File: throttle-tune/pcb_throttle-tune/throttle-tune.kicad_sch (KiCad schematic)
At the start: 48 parts, among them IC1 ATMEGA8A-P, J1 Screw_Terminal_01x03, J10 9V supply / small battery, J2 Screw_Terminal_01x03, J3 Screw_Terminal_01x03, J4 Screw_Terminal_01x03, J5 Conn_01x03_Pin, J6 UART, J7 gpio-reserve, J8 gpio-reserve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

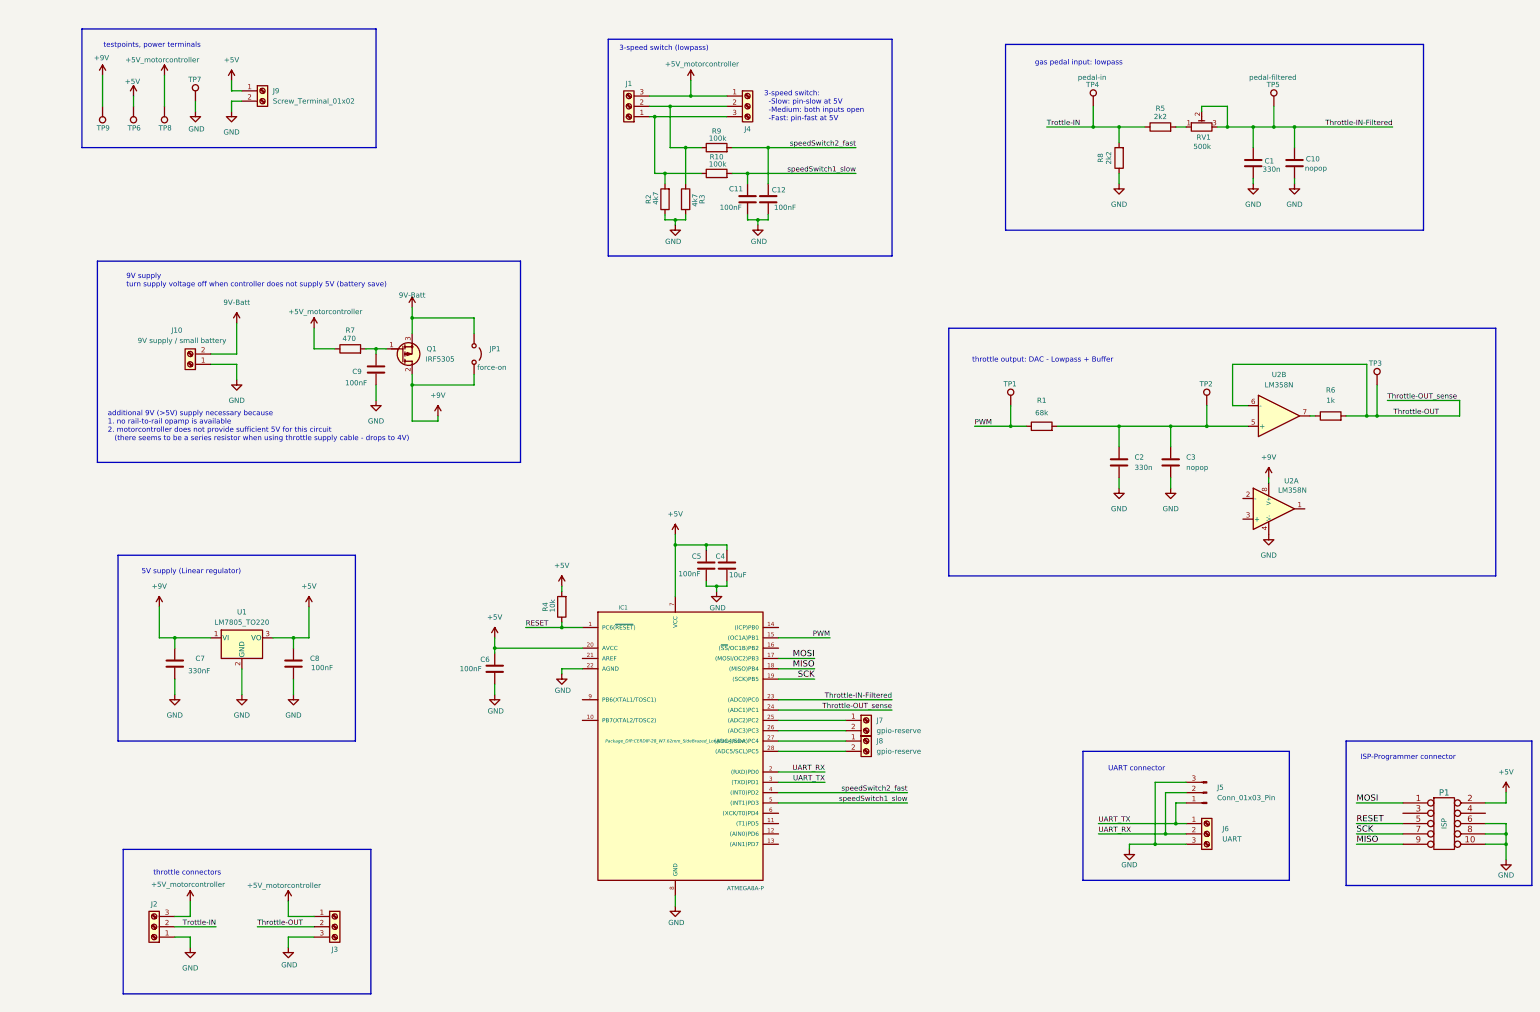
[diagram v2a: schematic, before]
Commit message: pcb: arrange components
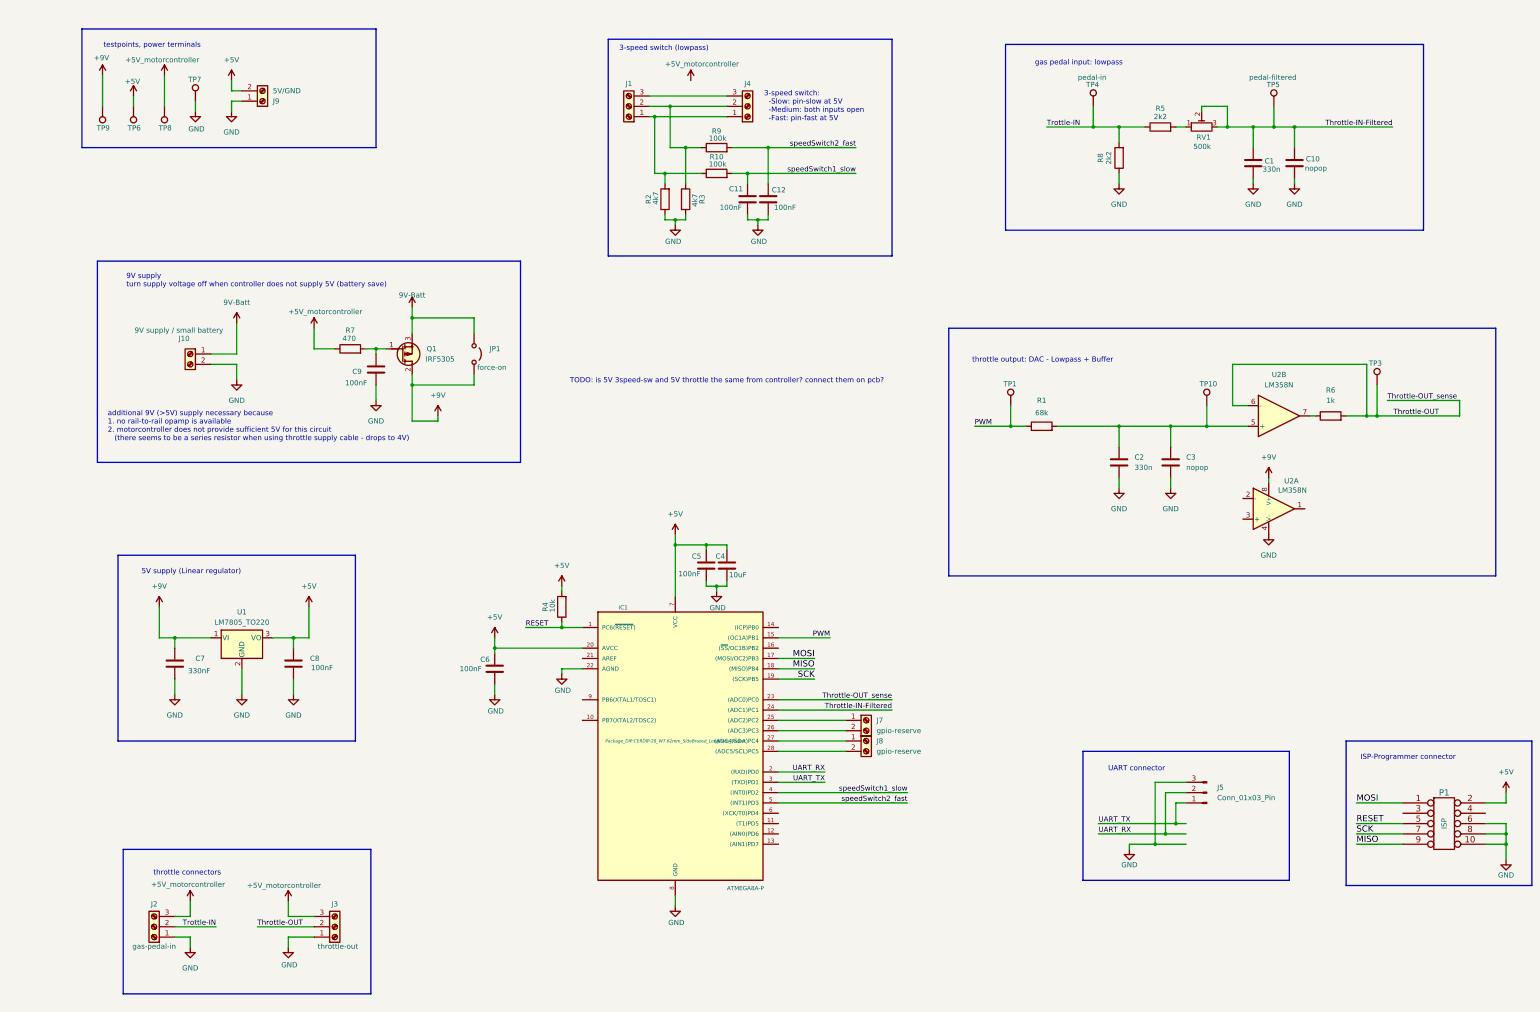
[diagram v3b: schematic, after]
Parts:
- removed J6: UART, TerminalBlock:TerminalBlock_bornier-2_P5.08mm, symbol Connector:Screw_Terminal_01x03
- J1: value Screw_Terminal_01x03 -> 3speedSw-in
- J2: value Screw_Terminal_01x03 -> gas-pedal-in
- J3: value Screw_Terminal_01x03 -> throttle-out
- J4: value Screw_Terminal_01x03 -> 3speedSw-out
- J5: footprint Connector_PinHeader_1.00mm:PinHeader_1x03_P1.00mm_Vertical -> Connector_PinHeader_2.54mm:PinHeader_1x03_P2.54mm_Vertical
- J9: value Screw_Terminal_01x02 -> 5V/GND
- JP1: footprint Connector_PinHeader_1.00mm:PinHeader_1x02_P1.00mm_Vertical -> Jumper_AKL:Jumper_P2.54mm_D0.7mm
- Q1: footprint Package_TO_SOT_THT:TO-220F-3_Vertical -> Package_TO_SOT_THT:TO-220-3_Vertical
- RV1: footprint Resistor_THT:R_Axial_DIN0207_L6.3mm_D2.5mm_P10.16mm_Horizontal -> Potentiometer_THT:Potentiometer_Piher_PT-10-V10_Vertical
- TP1: value TestPoint -> PWM
- TP10: renamed from TP2; value TestPoint -> DAC
- TP3: value TestPoint -> Throttle-Out
- TP7: value TestPoint -> GND
- TP8: value TestPoint -> 5V controller
- TP9: value TestPoint -> 9V
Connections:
- net +5V: now also J9.2 (Pin_2); no longer J9.1 (Pin_1)
- net +5V_motorcontroller: now also J3.3 (Pin_3); no longer J1.3 (Pin_3), J3.1 (Pin_1), J4.1 (Pin_1)
- net 9V-Batt: now also J10.1 (Pin_1); no longer J10.2 (Pin_2)
- net GND: now also J10.2 (Pin_2), J3.1 (Pin_1), J9.1 (Pin_1); no longer J10.1 (Pin_1), J3.3 (Pin_3), J9.2 (Pin_2)
- net Throttle-IN-Filtered: now also IC1.24 ((ADC1)PC1); no longer IC1.23 ((ADC0)PC0)
- net Throttle-OUT: now also IC1.23 ((ADC0)PC0); no longer IC1.24 ((ADC1)PC1)
- net speedSwitch1_slow: now also IC1.4 ((INT0)PD2); no longer IC1.5 ((INT1)PD3)
- net speedSwitch2_fast: now also IC1.5 ((INT1)PD3); no longer IC1.4 ((INT0)PD2)
- net at J1.1 (Pin_1), R10.1, R2.2: now also J4.1 (Pin_1); no longer J4.3 (Pin_3)
- new net: J1.3 (Pin_3), J4.3 (Pin_3)
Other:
- note added: "TODO: is 5V 3speed-sw and 5V throttle the same from controller? connect them on pcb?"
- moved on the sheet: J10
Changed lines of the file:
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@@
 	)
 	(junction
-		(at 172.72 38.1)
-		(diameter 0)
-		(color 0 0 0 0)
-	)
-	(junction
 		(at 104.14 109.22)
 		(diameter 0)
@@
 	(wire
 		(pts
-			(xy 172.72 34.29) (xy 172.72 38.1)
-		)
-		(stroke
-			(width 0)
-			(type default)
-		)
-	)
-	(wire
-		(pts
 			(xy 278.13 45.72) (xy 278.13 49.53)
 		)
@@
 	(wire
 		(pts
-			(xy 162.56 38.1) (xy 172.72 38.1)
+			(xy 162.56 38.1) (xy 181.61 38.1)
 		)
 		(stroke
@@
 	(wire
 		(pts
-			(xy 172.72 38.1) (xy 181.61 38.1)
-		)
-		(stroke
-			(width 0)
-			(type default)
-		)
-	)
-	(wire
-		(pts
 			(xy 186.69 68.58) (xy 189.23 68.58)
 		)
@@
 		)
 	)
+	(text "TODO: is 5V 3speed-sw and 5V throttle the same from controller? connect them on pcb?"
+		(exclude_from_sim no)
+		(at 181.61 108.204 0)
+		(effects
+			(font
+				(size 1.27 1.27)
+			)
+		)
+	)
 	(text "throttle connectors\n"
 		(exclude_from_sim no)
@@
 	)
 	(label "speedSwitch1_slow"
-		(at 226.06 212.09 180)
+		(at 226.06 209.55 180)
 		(fields_autoplaced yes)
 		(effects
@@
 	)
 	(label "speedSwitch2_fast"
-		(at 226.06 209.55 180)
+		(at 226.06 212.09 180)
 		(fields_autoplaced yes)
 		(effects
@@
 	)
 	(label "Throttle-IN-Filtered"
-		(at 222.25 186.69 180)
+		(at 222.25 189.23 180)
 		(fields_autoplaced yes)
 		(effects
@@
 	)
 	(label "Throttle-OUT_sense"
-		(at 222.25 189.23 180)
+		(at 222.25 186.69 180)
 		(fields_autoplaced yes)
 		(effects
@@
 			)
 		)
-		(property "Value" "TestPoint"
+		(property "Value" "5V controller"
 			(at 46.99 47.244 0)
 			(effects
@@
 		(on_board yes)
 		(dnp no)
-		(property "Reference" "TP2"
+		(property "Reference" "TP10"
 			(at 297.942 108.966 0)
 			(effects
@@
 			)
 		)
-		(property "Value" "TestPoint"
+		(property "Value" "DAC"
 			(at 302.26 112.2679 0)
 			(effects
@@
 			(project "throttle-tune"
 				(path "/54596f3c-134d-419d-8b8d-e3d4fb1ac7e3"
-					(reference "TP2")
+					(reference "TP10")
 					(unit 1)
 				)
@@
 	(symbol
 		(lib_id "Connector:Screw_Terminal_01x02")
-		(at 67.31 36.83 0)
+		(at 67.31 39.37 0)
+		(mirror x)
 		(unit 1)
 		(exclude_from_sim no)
@@
 		(on_board yes)
 		(dnp no)
-		(fields_autoplaced yes)
 		(property "Reference" "J9"
-			(at 69.85 36.8299 0)
+			(at 69.85 39.3701 0)
 			(effects
 				(font
@@
 			)
 		)
-		(property "Value" "Screw_Terminal_01x02"
-			(at 69.85 39.3699 0)
+		(property "Value" "5V/GND"
+			(at 69.85 36.8301 0)
 			(effects
 				(font
@@
 		)
 		(property "Footprint" "TerminalBlock:TerminalBlock_bornier-2_P5.08mm"
-			(at 67.31 36.83 0)
+			(at 67.31 39.37 0)
 			(effects
 				(font
@@
 		)
 		(property "Datasheet" "~"
-			(at 67.31 36.83 0)
+			(at 67.31 39.37 0)
 			(effects
 				(font
@@
 		)
 		(property "Description" "Generic screw terminal, single row, 01x02, script generated (kicad-library-utils/schlib/autogen/connector/)"
-			(at 67.31 36.83 0)
+			(at 67.31 39.37 0)
 			(effects
 				(font
@@
 			)
 		)
-		(property "Footprint" "Package_TO_SOT_THT:TO-220F-3_Vertical"
+		(property "Footprint" "Package_TO_SOT_THT:TO-220-3_Vertical"
 			(at 106.68 104.14 0)
 			(effects
@@
 	)
 	(symbol
-		(lib_id "Connector:Screw_Terminal_01x03")
-		(at 299.72 219.71 0)
-		(unit 1)
-		(exclude_from_sim no)
-		(in_bom yes)
-		(on_board yes)
-		(dnp no)
-		(fields_autoplaced yes)
-		(property "Reference" "J6"
-			(at 303.53 218.4399 0)
-			(effects
-				(font
-					(size 1.27 1.27)
-				)
-				(justify left)
-			)
-		)
-		(property "Value" "UART"
-			(at 303.53 220.9799 0)
-			(effects
-				(font
-					(size 1.27 1.27)
-				)
-				(justify left)
-			)
-		)
-		(property "Footprint" "TerminalBlock:TerminalBlock_bornier-2_P5.08mm"
-			(at 299.72 219.71 0)
-			(effects
-				(font
-					(size 1.27 1.27)
-				)
-				(hide yes)
-			)
-		)
-		(property "Datasheet" "~"
-			(at 299.72 219.71 0)
-			(effects
-				(font
-					(size 1.27 1.27)
-				)
-				(hide yes)
-			)
-		)
-		(property "Description" "Generic screw terminal, single row, 01x03, script generated (kicad-library-utils/schlib/autogen/connector/)"
-			(at 299.72 219.71 0)
-			(effects
-				(font
-					(size 1.27 1.27)
-				)
-				(hide yes)
-			)
-		)
-		(pin "1"
-		)
-		(pin "2"
-		)
-		(pin "3"
-		)
-		(instances
-			(project ""
-				(path "/54596f3c-134d-419d-8b8d-e3d4fb1ac7e3"
-					(reference "J6")
-					(unit 1)
-				)
-			)
-		)
-	)
-	(symbol
 		(lib_id "power:GND")
 		(at 168.91 69.85 0)
@@
 			)
 		)
-		(property "Value" "TestPoint"
+		(property "Value" "GND"
 			(at 46.99 32.766 0)
 			(effects
@@
 			)
 		)
-		(property "Footprint" "Connector_PinHeader_1.00mm:PinHeader_1x02_P1.00mm_Vertical"
+		(property "Footprint" "Jumper_AKL:Jumper_P2.54mm_D0.7mm"
 			(at 119.38 101.6 0)
 			(effects
@@
 		(lib_id "Connector:Screw_Terminal_01x03")
 		(at 85.09 242.57 0)
+		(mirror x)
 		(unit 1)
 		(exclude_from_sim no)
@@
 		(dnp no)
 		(property "Reference" "J3"
-			(at 85.09 248.158 0)
+			(at 85.09 236.982 0)
 			(effects
 				(font
@@
 			)
 		)
-		(property "Value" "Screw_Terminal_01x03"
-			(at 86.106 248.412 0)
+		(property "Value" "throttle-out"
+			(at 85.852 247.396 0)
 			(effects
 				(font
 					(size 1.27 1.27)
 				)
-				(hide yes)
 			)
 		)
@@
 			)
 		)
-		(property "Value" "TestPoint"
+		(property "Value" "Throttle-Out"
 			(at 344.17 107.1879 0)
 			(effects
@@
 			)
 		)
-		(property "Value" "TestPoint"
+		(property "Value" "PWM"
 			(at 247.65 107.696 0)
 			(effects
@@
 			)
 		)
-		(property "Value" "TestPoint"
+		(property "Value" "9V"
 			(at 31.75 47.244 0)
 			(effects
@@
 			)
 		)
-		(property "Footprint" "Connector_PinHeader_1.00mm:PinHeader_1x03_P1.00mm_Vertical"
+		(property "Footprint" "Connector_PinHeader_2.54mm:PinHeader_1x03_P2.54mm_Vertical"
 			(at 299.72 209.55 0)
 			(effects
@@
 			)
 		)
-		(property "Value" "Screw_Terminal_01x03"
+		(property "Value" "3speedSw-in"
 			(at 156.464 34.798 0)
 			(effects
@@
 	(symbol
 		(lib_id "Connector:Screw_Terminal_01x02")
-		(at 49.53 104.14 180)
+		(at 49.53 101.6 0)
+		(mirror y)
 		(unit 1)
 		(exclude_from_sim no)
@@
 		(dnp no)
 		(property "Reference" "J10"
-			(at 46.228 95.758 0)
+			(at 48.006 97.79 0)
 			(effects
 				(font
@@
 		)
 		(property "Value" "9V supply / small battery"
-			(at 47.498 98.298 0)
+			(at 46.736 95.758 0)
 			(effects
 				(font
@@
 		)
 		(property "Footprint" "TerminalBlock:TerminalBlock_bornier-2_P5.08mm"
-			(at 49.53 104.14 0)
+			(at 49.53 101.6 0)
 			(effects
 				(font
@@
 		)
 		(property "Datasheet" "~"
-			(at 49.53 104.14 0)
+			(at 49.53 101.6 0)
 			(effects
 				(font
@@
 		)
 		(property "Description" "Generic screw terminal, single row, 01x02, script generated (kicad-library-utils/schlib/autogen/connector/)"
-			(at 49.53 104.14 0)
+			(at 49.53 101.6 0)
 			(effects
 				(font
@@
 		(lib_id "Connector:Screw_Terminal_01x03")
 		(at 186.69 40.64 0)
+		(mirror x)
 		(unit 1)
 		(exclude_from_sim no)
@@
 		(dnp no)
 		(property "Reference" "J4"
-			(at 186.69 46.228 0)
+			(at 186.69 35.052 0)
 			(effects
 				(font
@@
 			)
 		)
-		(property "Value" "Screw_Terminal_01x03"
-			(at 187.706 46.482 0)
+		(property "Value" "3speedSw-out"
+			(at 187.706 34.798 0)
 			(effects
 				(font
@@
 			)
 		)
-		(property "Value" "Screw_Terminal_01x03"
-			(at 39.624 236.728 0)
+		(property "Value" "gas-pedal-in"
+			(at 40.64 247.396 0)
 			(effects
 				(font
 					(size 1.27 1.27)
 				)
-				(hide yes)
 			)
 		)
@@
 			)
 		)
-		(property "Footprint" "Resistor_THT:R_Axial_DIN0207_L6.3mm_D2.5mm_P10.16mm_Horizontal"
+		(property "Footprint" "Potentiometer_THT:Potentiometer_Piher_PT-10-V10_Vertical"
 			(at 298.45 45.72 0)
 			(effects

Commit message: pcb: finish layout, pcb2gcode, adj pins - milled pcb
milled pcb and populated, works well but
error with P-channel mosfet (missing NPN driver)
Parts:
- added C13: 100nF, Capacitor_THT:C_Disc_D7.0mm_W2.5mm_P5.00mm, symbol Device:C
- added R11: 100k, Resistor_THT:R_Axial_DIN0207_L6.3mm_D2.5mm_P10.16mm_Horizontal, symbol Device:R
- J5: value Conn_01x03_Pin -> UART [TX, RX, GND]
- J8: value gpio-reserve -> reserve, reverse-sw
- R7: value 470 -> 1k
- TP6: value TestPoint -> 5V
- U1: value LM7805_TO220 -> LM7805
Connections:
- net GND: now also P1.3, P1.4, C13.2
- net REV-in: now reaches J8.2 (Pin_2)
- net REV-in: now also R11.1; no longer IC1.28 ((ADC5/SCL)PC5)
- new net Reverse-sw: C13.1, IC1.28 ((ADC5/SCL)PC5), R11.2
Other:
- note added: "Reverse switch"
- note added: "TODO: - is 5V 3speed-sw and 5V throttle the same from controller? connect them on pcb? - measure reverse switch voltage"
- note added: "note: 3 usually not connected"
- note removed: "TODO: is 5V 3speed-sw and 5V throttle the same from controller? connect them on pcb?"
- title: (none) -> Throttle-Tune
- moved on the sheet: J7, J8
